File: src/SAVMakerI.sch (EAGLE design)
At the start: 35 parts, among them J2 AVR_SPI_PRG_6PTH, U1 ATMEGA32U4-AU, Y1 RESONATORSMD

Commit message: Added oscillator replacing the resonator.
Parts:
- removed Y1: RESONATORSMD, sparkfun_2:RESONATORSMD
- added C15, C16: 18pF, sparkfun_2:CAP1206
- added Q1: CSM-3X-CRYSTALCSM-3X, fmc:CSM-3X-CRYSTALCSM-3X
- renumbered A to B
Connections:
- net GND: now also C15.2, C16.2; no longer Y1.2
- net N$3: now also C16.1, Q1.2; no longer Y1.3
- net N$4: now also C15.1, Q1.1; no longer Y1.1
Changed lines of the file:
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@@
 <?xml version="1.0" encoding="utf-8"?>
 <!DOCTYPE eagle SYSTEM "eagle.dtd">
-<eagle version="7.0.0">
+<eagle version="7.5.0">
 <drawing>
 <settings>
@@
 <classes>
 <class number="0" name="default" width="0" drill="0">
-<clearance class="0" value="0.1778"/>
 </class>
 <class number="1" name="vcc" width="0.254" drill="0">
@@
 <part name="J2" library="SparkFun" deviceset="AVR_SPI_PRG_6" device="PTH"/>
 <part name="S1" library="SparkFun" deviceset="TAC_SWITCH" device="SMD"/>
-<part name="Y1" library="sparkfun_2" deviceset="RESONATOR" device="SMD"/>
-<part name="GND4" library="SparkFun" deviceset="GND" device=""/>
-<part name="A" library="fmc" deviceset="BOARD_INFO_BMP_20" device="" value="SAV Maker I"/>
+<part name="B" library="fmc" deviceset="BOARD_INFO_BMP_20" device="" value="SAV Maker I"/>
 <part name="R1" library="adafruit" deviceset="R-US_" device="R1206" value="1M"/>
 <part name="C7" library="sparkfun_2" deviceset="CAP" device="1206" value="4.7nF"/>
 <part name="GND8" library="supply1" deviceset="GND" device="" value="GNDS"/>
+<part name="GND10" library="SparkFun" deviceset="GND" device=""/>
+<part name="C15" library="sparkfun_2" deviceset="CAP" device="1206" value="18pF"/>
+<part name="C16" library="sparkfun_2" deviceset="CAP" device="1206" value="18pF"/>
+<part name="GND22" library="SparkFun" deviceset="GND" device=""/>
+<part name="Q1" library="fmc" deviceset="CSM-3X-CRYSTAL" device="CSM-3X"/>
 </parts>
 <sheets>
@@
 <instance part="J2" gate="G$1" x="50.8" y="66.04"/>
 <instance part="S1" gate="S" x="129.54" y="50.8" rot="R90"/>
-<instance part="Y1" gate="G$1" x="182.88" y="114.3"/>
-<instance part="GND4" gate="1" x="182.88" y="104.14"/>
-<instance part="A" gate="G$1" x="241.3" y="15.24"/>
+<instance part="B" gate="G$1" x="241.3" y="15.24"/>
 <instance part="R1" gate="G$1" x="86.36" y="111.76" rot="R180"/>
 <instance part="C7" gate="G$1" x="86.36" y="116.84" rot="R90"/>
 <instance part="GND8" gate="1" x="93.98" y="104.14"/>
+<instance part="GND10" gate="1" x="190.5" y="101.6" rot="MR0"/>
+<instance part="C15" gate="G$1" x="175.26" y="106.68" smashed="yes">
+<attribute name="NAME" x="169.164" y="109.601" size="1.778" layer="95"/>
+<attribute name="VALUE" x="167.64" y="104.521" size="1.778" layer="96"/>
+</instance>
+<instance part="C16" gate="G$1" x="190.5" y="106.68" smashed="yes">
+<attribute name="NAME" x="192.024" y="109.601" size="1.778" layer="95"/>
+<attribute name="VALUE" x="193.04" y="104.521" size="1.778" layer="96"/>
+</instance>
+<instance part="GND22" gate="1" x="175.26" y="101.6" rot="MR0"/>
+<instance part="Q1" gate="G$1" x="182.88" y="111.76" smashed="yes">
+<attribute name="NAME" x="182.118" y="115.316" size="1.6764" layer="95" ratio="11"/>
+<attribute name="VALUE" x="191.77" y="114.046" size="1.4224" layer="96" ratio="12"/>
+</instance>
 </instances>
 <busses>
@@
 <net name="N$3" class="0">
 <segment>
-<wire x1="185.42" y1="149.86" x2="210.82" y2="149.86" width="0.1524" layer="91"/>
+<wire x1="190.5" y1="149.86" x2="210.82" y2="149.86" width="0.1524" layer="91"/>
 <pinref part="U1" gate="G$1" pin="XTAL2"/>
-<wire x1="185.42" y1="149.86" x2="185.42" y2="114.3" width="0.1524" layer="91"/>
-<pinref part="Y1" gate="G$1" pin="3"/>
+<pinref part="C16" gate="G$1" pin="1"/>
+<pinref part="Q1" gate="G$1" pin="2"/>
+<wire x1="190.5" y1="149.86" x2="190.5" y2="111.76" width="0.1524" layer="91"/>
+<junction x="190.5" y="111.76"/>
 </segment>
 </net>
@@
 <wire x1="210.82" y1="157.48" x2="180.34" y2="157.48" width="0.1524" layer="91"/>
 <pinref part="U1" gate="G$1" pin="XTAL1"/>
-<wire x1="180.34" y1="114.3" x2="180.34" y2="157.48" width="0.1524" layer="91"/>
-<pinref part="Y1" gate="G$1" pin="1"/>
+<wire x1="180.34" y1="157.48" x2="180.34" y2="116.84" width="0.1524" layer="91"/>
+<wire x1="180.34" y1="116.84" x2="175.26" y2="116.84" width="0.1524" layer="91"/>
+<pinref part="C15" gate="G$1" pin="1"/>
+<pinref part="Q1" gate="G$1" pin="1"/>
+<wire x1="175.26" y1="116.84" x2="175.26" y2="111.76" width="0.1524" layer="91"/>
+<junction x="175.26" y="111.76"/>
 </segment>
 </net>
@@
 </segment>
 <segment>
-<pinref part="Y1" gate="G$1" pin="2"/>
-<pinref part="GND4" gate="1" pin="GND"/>
-</segment>
-</net>
+<pinref part="C15" gate="G$1" pin="2"/>
+<pinref part="GND22" gate="1" pin="GND"/>
+</segment>
+<segment>
+<pinref part="C16" gate="G$1" pin="2"/>
+<pinref part="GND10" gate="1" pin="GND"/>
+</segment>
+</net>

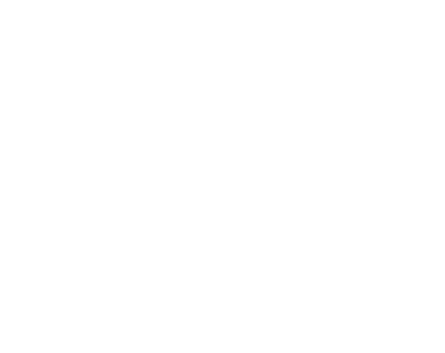
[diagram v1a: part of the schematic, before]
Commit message: Minor modifications to routes.
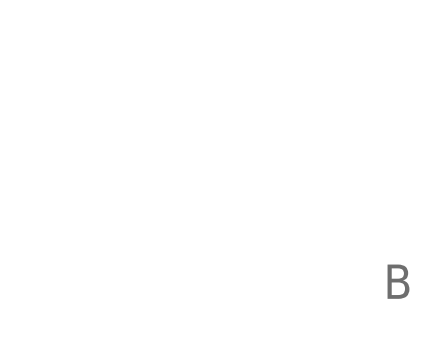
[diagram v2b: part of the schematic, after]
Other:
- note added: "B"
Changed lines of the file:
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@@
 <wire x1="15.24" y1="175.26" x2="137.16" y2="175.26" width="0.1524" layer="94"/>
 <text x="292.1" y="25.4" size="3.81" layer="97" ratio="15">SAV Maker I - by fm</text>
+<text x="383.794" y="6.604" size="3.81" layer="95">B</text>
 </plain>
 <instances>
